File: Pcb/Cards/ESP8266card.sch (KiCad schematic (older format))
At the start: 16 parts, among them P1 Debug-SoftSerial-FTDI, P2 ESP-Programming-FTDI, P3 CA6_CONN_01X10, U1 ESP-12E/F

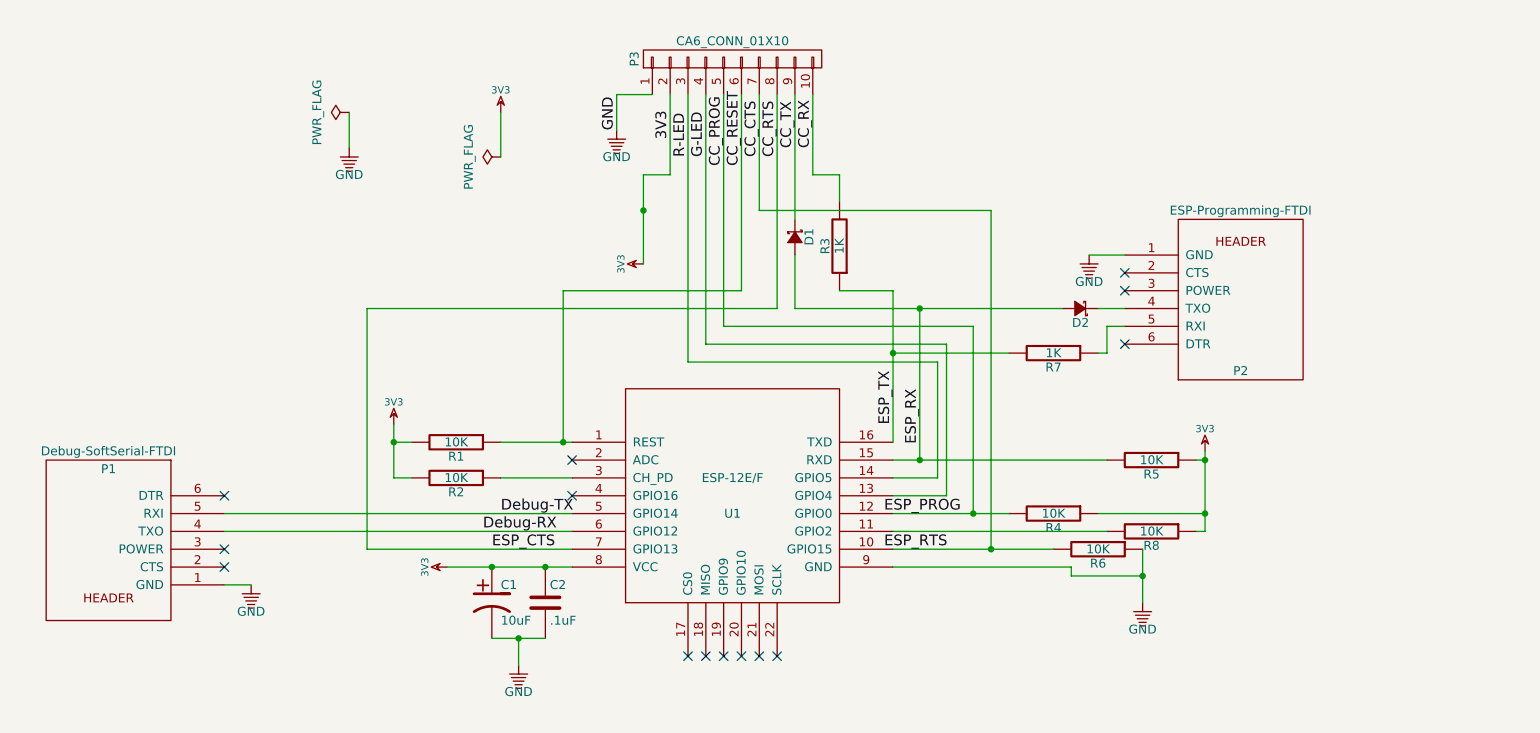
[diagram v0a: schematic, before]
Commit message: 1st commit with completed schematic and routed board.  Added 1K on ESP RX back in (easy to short later if it causes problems). Used 12 mil Power & Gnd and 6 mil remaining traces.  1x10 CA6_Com_connector is properly on the bottom, but FTDI headers and unpopulated.  We'll need to check that case has room when they are populated.  I wasn't sure how to get air-wires for Gnd's on headers to go away, so I added via's on the pin and separately (check and correct if needed).  Card outline is .05" less than CA6 board on the right and bottom for case clearance.  Did not start gerber process.
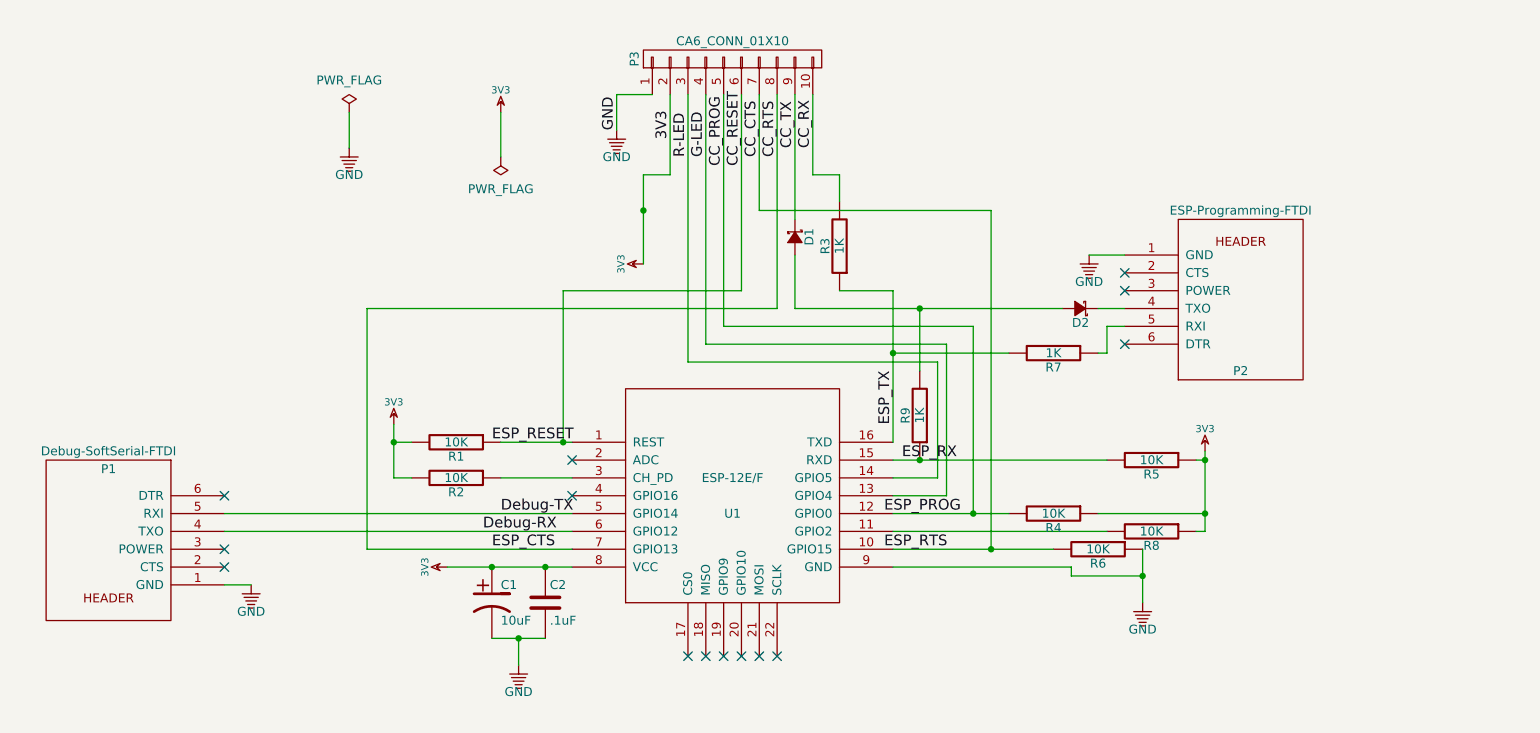
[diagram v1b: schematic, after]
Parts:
- added R9: 1K, CA6:SM0603_Resistor, symbol R
- U1: footprint CA6:ESP-12E -> CA6:ESP-12E-F-no-bottom-pads
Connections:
- net ESP_RX: now also R9.1; no longer D1.2 (A), D2.2 (A)
- new net: D1.2 (A), D2.2 (A), R9.2
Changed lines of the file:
@@
 LIBS:contrib
 LIBS:valves
-LIBS:w_rtx
-LIBS:ESP8266
-LIBS:74xgxx
-LIBS:ac-dc
-LIBS:actel
-LIBS:allegro
-LIBS:Altera
-LIBS:analog_devices
-LIBS:battery_management
-LIBS:bbd
-LIBS:bosch
-LIBS:brooktre
-LIBS:cmos_ieee
-LIBS:dc-dc
-LIBS:diode
-LIBS:elec-unifil
-LIBS:ESD_Protection
-LIBS:ftdi
-LIBS:gennum
-LIBS:graphic
-LIBS:hc11
-LIBS:ir
-LIBS:Lattice
-LIBS:logo
-LIBS:maxim
-LIBS:mechanical
-LIBS:microchip_dspic33dsc
-LIBS:microchip_pic10mcu
-LIBS:microchip_pic12mcu
-LIBS:microchip_pic16mcu
-LIBS:microchip_pic18mcu
-LIBS:microchip_pic32mcu
-LIBS:motor_drivers
-LIBS:motors
-LIBS:msp430
-LIBS:nordicsemi
-LIBS:NXP
-LIBS:nxp_1
-LIBS:nxp_armmcu
-LIBS:onsemi
-LIBS:Oscillators
-LIBS:Power_Management
-LIBS:powerint
-LIBS:pspice
-LIBS:references
-LIBS:relays
-LIBS:rfcom
-LIBS:sensors
-LIBS:silabs
-LIBS:stm8
-LIBS:stm32
-LIBS:supertex
-LIBS:switches
-LIBS:transf
-LIBS:triac_thyristor
-LIBS:ttl_ieee
-LIBS:video
-LIBS:wiznet
-LIBS:Worldsemi
-LIBS:Xicor
-LIBS:zetex
-LIBS:Zilog
 LIBS:ESP8266card-cache
 EELAYER 25 0
@@
 	7650 2900 7500 2900
 Wire Wire Line
-	3550 3550 3550 3650
-Wire Wire Line
-	3550 3650 3550 3850
+	3550 3550 3550 3850
 Connection ~ 3550 3650
 $Comp
@@
 $EndComp
 Wire Wire Line
-	7750 4250 7750 4400
-Wire Wire Line
-	7750 4400 7750 4550
+	7750 4250 7750 4550
 $Comp
 L R R8
@@
 $EndComp
 Wire Wire Line
-	8100 3700 8100 3750
-Wire Wire Line
-	8100 3750 8100 4050
-Wire Wire Line
-	8100 4050 8100 4150
+	8100 3700 8100 4150
 Connection ~ 8100 4050
 Connection ~ 8100 3750
@@
 $EndComp
 Wire Wire Line
-	3850 4350 4100 4350
-Wire Wire Line
-	4100 4350 4400 4350
-Wire Wire Line
-	4400 4350 4550 4350
+	3850 4350 4550 4350
 Connection ~ 4400 4350
 Wire Wire Line
-	4100 4750 4250 4750
-Wire Wire Line
-	4250 4750 4400 4750
+	4100 4750 4400 4750
 $Comp
 L GND #PWR04
@@
 F 3 "" H 4150 2050 50  0000 C CNN
 	1    4150 2050
-	0    -1   -1   0
+	-1   0    0    1
 $EndComp
 $Comp
@@
 	5200 1700 5200 3200
 Wire Wire Line
-	6350 2800 6350 3150
-Wire Wire Line
-	6350 3150 6350 3650
+	6350 2800 6350 3650
 Text Label 6350 3550 1    60   ~ 0
 ESP_TX
@@
 NoConn ~ 2600 4350
 Connection ~ 6500 3750
-Text Label 6500 3350 3    60   ~ 0
-ESP_RX
 Wire Wire Line
 	5000 1700 4800 1700
@@
 	5100 2150 4950 2150
 Wire Wire Line
-	4950 2150 4950 2350
-Wire Wire Line
-	4950 2350 4950 2650
+	4950 2150 4950 2650
 Connection ~ 4950 2350
 Wire Wire Line
@@
 	6350 2800 6050 2800
 Wire Wire Line
-	5800 2900 6500 2900
-Wire Wire Line
-	6500 2900 7300 2900
+	5800 2900 7300 2900
 Connection ~ 6500 2900
 Wire Wire Line
 	5800 2600 5800 2900
-Wire Wire Line
-	6500 3750 6500 2900
 Wire Wire Line
 	6350 3850 6600 3850
@@
 F 0 "U1" H 5450 3850 50  0000 C CNN
 F 1 "ESP-12E/F" H 5450 4050 50  0000 C CNN
-F 2 "CA6:ESP-12E" H 5450 3950 50  0001 C CNN
+F 2 "CA6:ESP-12E-F-no-bottom-pads" H 5450 3950 50  0001 C CNN
 F 3 "" H 5450 3950 50  0001 C CNN
 	1    5450 3950
@@
 	6050 2150 6050 2300
 Wire Wire Line
-	6350 4250 6900 4250
-Wire Wire Line
-	6900 4250 7250 4250
+	6350 4250 7250 4250
 Wire Wire Line
 	3650 3650 3550 3650
@@
 	4550 3850 4150 3850
 Wire Wire Line
-	4150 3650 4500 3650
-Wire Wire Line
-	4500 3650 4550 3650
+	4150 3650 4550 3650
 Wire Wire Line
 	8050 3750 8100 3750
 Wire Wire Line
-	6350 3750 6500 3750
-Wire Wire Line
-	6500 3750 7550 3750
+	6350 3750 7550 3750
 Wire Wire Line
 	7500 4050 8100 4050
 Wire Wire Line
-	6350 4050 6800 4050
-Wire Wire Line
-	6800 4050 7000 4050
+	6350 4050 7000 4050
 Wire Wire Line
 	5900 1700 5900 2150
@@
 F 3 "" H 3300 1800 50  0000 C CNN
 	1    3300 1800
-	0    -1   -1   0
+	1    0    0    -1
 $EndComp
 $Comp
@@
 	1    0    0    -1
 $EndComp
+$Comp
+L R R9
+U 1 1 58C41CF1
+P 6500 3500
+F 0 "R9" V 6580 3500 50  0000 C CNN
+F 1 "1K" V 6500 3500 50  0000 C CNN
+F 2 "CA6:SM0603_Resistor" V 6430 3500 50  0001 C CNN
+F 3 "" H 6500 3500 50  0000 C CNN
+	1    6500 3500
+	-1   0    0    1
+$EndComp
+Wire Wire Line
+	6500 3250 6500 2900
+Text Label 6400 3750 0    60   ~ 0
+ESP_RX
+Text Label 4100 3650 0    60   ~ 0
+ESP_RESET
 $EndSCHEMATC

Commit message: Fix some drc issues
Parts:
- P2: symbol FTDI -> FTDI-RESCUE-ESP8266card
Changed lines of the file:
@@
 EESchema Schematic File Version 2
+LIBS:ESP8266card-rescue
 LIBS:CA6
 LIBS:power
@@
 $EndComp
 $Comp
-L FTDI P2
+L FTDI-RESCUE-ESP8266card P2
 U 1 1 58C10A25
 P 8300 2850
@@
 L GND #PWR02
 U 1 1 58C14094
-P 4800 1900
-F 0 "#PWR02" H 4800 1650 50  0001 C CNN
-F 1 "GND" H 4800 1750 50  0000 C CNN
-F 2 "" H 4800 1900 50  0000 C CNN
-F 3 "" H 4800 1900 50  0000 C CNN
-	1    4800 1900
+P 4950 1900
+F 0 "#PWR02" H 4950 1650 50  0001 C CNN
+F 1 "GND" H 4950 1750 50  0000 C CNN
+F 2 "" H 4950 1900 50  0000 C CNN
+F 3 "" H 4950 1900 50  0000 C CNN
+	1    4950 1900
 	1    0    0    -1
 $EndComp
@@
 Connection ~ 4100 4350
 $Comp
-L PWR_FLAG #FLG05
-U 1 1 58C165F7
-P 4150 2050
-F 0 "#FLG05" H 4150 2145 50  0001 C CNN
-F 1 "PWR_FLAG" H 4150 2230 50  0000 C CNN
-F 2 "" H 4150 2050 50  0000 C CNN
-F 3 "" H 4150 2050 50  0000 C CNN
-	1    4150 2050
-	-1   0    0    1
-$EndComp
-$Comp
 L CONN_01X10 P3
 U 1 1 58BE5BC6
@@
 $EndComp
 Wire Wire Line
-	5100 1700 5100 2150
+	5100 2150 5100 1700
 Wire Wire Line
 	5300 1700 5300 3100
@@
 Wire Wire Line
 	5800 1700 5800 2400
-Text Label 4800 1900 1    60   ~ 0
-GND
-Text Label 5100 1950 1    60   ~ 0
-3V3
-Text Label 5900 2000 1    60   ~ 0
+Text Label 5900 2100 1    60   ~ 0
 CC_RX
-Text Label 5200 2050 1    60   ~ 0
+Text Label 5200 2100 1    60   ~ 0
 R-LED
-Text Label 5800 2000 1    60   ~ 0
+Text Label 5800 2100 1    60   ~ 0
 CC_TX
-Text Label 5300 2050 1    60   ~ 0
+Text Label 5300 2100 1    60   ~ 0
 G-LED
-Text Label 5700 2050 1    60   ~ 0
+Text Label 5700 2100 1    60   ~ 0
 CC_RTS
 Text Label 5500 2100 1    60   ~ 0
 CC_RESET
-Text Label 5600 2050 1    60   ~ 0
+Text Label 5600 2100 1    60   ~ 0
 CC_CTS
 Text Label 5400 2100 1    60   ~ 0
@@
 P 1950 4200
 F 0 "P1" H 1950 3800 50  0000 C CNN
-F 1 "Debug-SoftSerial-FTDI" H 1950 3700 50  0000 C CNN
+F 1 "Debug-SoftSerial-FTDI" H 1950 4600 50  0000 C CNN
 F 2 "CA6:SIL-6" H 1950 4200 50  0001 C CNN
 F 3 "DOCUMENTATION" H 1950 4200 50  0001 C CNN
@@
 	2600 4050 4550 4050
 $Comp
-L GND #PWR06
+L GND #PWR05
 U 1 1 58BF45F7
 P 2750 4450
-F 0 "#PWR06" H 2750 4200 50  0001 C CNN
+F 0 "#PWR05" H 2750 4200 50  0001 C CNN
 F 1 "GND" H 2750 4300 50  0000 C CNN
 F 2 "" H 2750 4450 50  0000 C CNN
@@
 	1    0    0    -1
 $EndComp
-Wire Wire Line
-	2750 4450 2600 4450
 Text Label 4150 4050 0    60   ~ 0
 Debug-TX
@@
 Connection ~ 6500 3750
 Wire Wire Line
-	5000 1700 4800 1700
-Wire Wire Line
-	4800 1700 4800 1900
-Wire Wire Line
-	5100 2150 4950 2150
-Wire Wire Line
-	4950 2150 4950 2650
-Connection ~ 4950 2350
+	5000 1700 4950 1700
+Wire Wire Line
+	4950 1700 4950 1900
+Wire Wire Line
+	4950 2150 5100 2150
 Wire Wire Line
 	5900 2150 6050 2150
@@
 	-1   0    0    1
 $EndComp
-$Comp
-L GND #PWR07
-U 1 1 58C2E8B7
-P 3300 2000
-F 0 "#PWR07" H 3300 1750 50  0001 C CNN
-F 1 "GND" H 3300 1850 50  0000 C CNN
-F 2 "" H 3300 2000 50  0000 C CNN
-F 3 "" H 3300 2000 50  0000 C CNN
-	1    3300 2000
-	1    0    0    -1
-$EndComp
-Wire Wire Line
-	4150 1800 4150 2050
-Wire Wire Line
-	3300 1800 3300 2000
 Wire Wire Line
 	7550 4150 6350 4150
@@
 	8100 4150 8050 4150
 $Comp
-L PWR_FLAG #FLG08
-U 1 1 58C32C54
-P 3300 1800
-F 0 "#FLG08" H 3300 1895 50  0001 C CNN
-F 1 "PWR_FLAG" H 3300 1980 50  0000 C CNN
-F 2 "" H 3300 1800 50  0000 C CNN
-F 3 "" H 3300 1800 50  0000 C CNN
-	1    3300 1800
-	1    0    0    -1
-$EndComp
-$Comp
-L 3V3 #PWR09
+L 3V3 #PWR06
 U 1 1 58C32ED5
-P 4950 2650
-F 0 "#PWR09" H 4950 2750 40  0001 C CNN
-F 1 "3V3" H 4950 2775 40  0000 C CNN
-F 2 "" H 4950 2650 60  0000 C CNN
-F 3 "" H 4950 2650 60  0000 C CNN
-	1    4950 2650
+P 4950 2150
+F 0 "#PWR06" H 4950 2250 40  0001 C CNN
+F 1 "3V3" H 4950 2275 40  0000 C CNN
+F 2 "" H 4950 2150 60  0000 C CNN
+F 3 "" H 4950 2150 60  0000 C CNN
+	1    4950 2150
 	0    -1   -1   0
 $EndComp
 $Comp
-L 3V3 #PWR010
-U 1 1 58C33748
-P 4150 1800
-F 0 "#PWR010" H 4150 1900 40  0001 C CNN
-F 1 "3V3" H 4150 1925 40  0000 C CNN
-F 2 "" H 4150 1800 60  0000 C CNN
-F 3 "" H 4150 1800 60  0000 C CNN
-	1    4150 1800
-	1    0    0    -1
-$EndComp
-$Comp
-L 3V3 #PWR011
+L 3V3 #PWR07
 U 1 1 58C341AF
 P 3550 3550
-F 0 "#PWR011" H 3550 3650 40  0001 C CNN
+F 0 "#PWR07" H 3550 3650 40  0001 C CNN
 F 1 "3V3" H 3550 3675 40  0000 C CNN
 F 2 "" H 3550 3550 60  0000 C CNN
@@
 $EndComp
 $Comp
-L 3V3 #PWR012
+L 3V3 #PWR08
 U 1 1 58C34BCB
 P 3850 4350
-F 0 "#PWR012" H 3850 4450 40  0001 C CNN
+F 0 "#PWR08" H 3850 4450 40  0001 C CNN
 F 1 "3V3" H 3850 4475 40  0000 C CNN
 F 2 "" H 3850 4350 60  0000 C CNN
@@
 $EndComp
 $Comp
-L 3V3 #PWR013
+L 3V3 #PWR09
 U 1 1 58C34C97
 P 8100 3700
-F 0 "#PWR013" H 8100 3800 40  0001 C CNN
+F 0 "#PWR09" H 8100 3800 40  0001 C CNN
 F 1 "3V3" H 8100 3825 40  0000 C CNN
 F 2 "" H 8100 3700 60  0000 C CNN
@@
 Text Label 4100 3650 0    60   ~ 0
 ESP_RESET
+Wire Wire Line
+	2750 4450 2600 4450
 $EndSCHEMATC

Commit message: Eliminated ground pour, changed FTDI headers to angled, corrected ESP-12E/F-no-bottom-pads to SMD pads, improved spacing near antenna, moved and shrank some text values
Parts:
- P1, P2: footprint CA6:SIL-6 -> Pin_Headers:Pin_Header_Angled_1x06_Pitch2.54mm
- P3: footprint Pin_Headers:Pin_Header_Straight_1x10_Pitch2.54mm -> Pin_Header_Straight_1x10_Pitch2.54mm
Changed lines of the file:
@@
 F 0 "P2" H 8300 2450 50  0000 C CNN
 F 1 "ESP-Programming-FTDI" H 8300 3350 50  0000 C CNN
-F 2 "CA6:SIL-6" H 8300 2850 50  0001 C CNN
+F 2 "Pin_Headers:Pin_Header_Angled_1x06_Pitch2.54mm" H 8300 2850 50  0001 C CNN
 F 3 "DOCUMENTATION" H 8300 2850 50  0001 C CNN
 	1    8300 2850
@@
 F 0 "P3" H 5450 2050 50  0000 C CNN
 F 1 "CA6_CONN_01X10" V 5550 1500 50  0000 C CNN
-F 2 "Pin_Headers:Pin_Header_Straight_1x10_Pitch2.54mm" H 5450 1500 50  0001 C CNN
+F 2 "Pin_Header_Straight_1x10_Pitch2.54mm" H 5450 1500 50  0001 C CNN
 F 3 "" H 5450 1500 50  0000 C CNN
 	1    5450 1500
@@
 F 0 "P1" H 1950 3800 50  0000 C CNN
 F 1 "Debug-SoftSerial-FTDI" H 1950 4600 50  0000 C CNN
-F 2 "CA6:SIL-6" H 1950 4200 50  0001 C CNN
+F 2 "Pin_Headers:Pin_Header_Angled_1x06_Pitch2.54mm" H 1950 4200 50  0001 C CNN
 F 3 "DOCUMENTATION" H 1950 4200 50  0001 C CNN
 	1    1950 4200

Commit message: Got rid of old 1x10 version and renamed cards2 to card, also fixed one text field
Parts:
- removed D1, D2: diode_schottky_20V_1A, CA6:DO-214AC(SMA), symbol diode_schottky_20V_1A
- removed P1: Debug-SoftSerial-FTDI, Pin_Headers:Pin_Header_Angled_1x06_Pitch2.54mm, symbol FTDI
- removed P3: CA6_CONN_01X10, Pin_Header_Straight_1x10_Pitch2.54mm, symbol CONN_01X10
- removed R3, R7, R9: 1K, CA6:SM0603_Resistor, symbol R
- removed R5: 10K, CA6:SM0603_Resistor, symbol R
- added J1: Debug_TX, CA6:Pin_Header_Angled_1x02_Pitch2.54mm, symbol CONN_01X02
- added J2: CA6_02X06, CA6:Pin_Header_Straight_2x06_Pitch2.54mm, symbol CONN_02X06
- added U1: SN74AHC1G08, CA6:SOT-23-5_GATE, symbol SN74AHC1G08
- added X1: HOLE, CA6:HOLE_3.0mm, symbol HOLE
- P1: renamed from P2; symbol FTDI-RESCUE-ESP8266card -> FTDI
- R3: renamed from R4; value 10K -> 4.7k
- R5: renamed from R1; value 10K -> 4.7k
- renumbered C2 to C1, C1 to C2, R8 to R1, R6 to R2, R2 to R4, U1 to U2
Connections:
- net ESP_TX is gone; now on net CC_RX: U2.16 (TXD)
- net 3V3: now also J2.2 (P2), U1.5 (VCC)
- net CC_CTS: now also J2.7 (P7)
- net CC_PROG: now also J2.5 (P5)
- net CC_RESET: now also J2.6 (P6)
- net CC_RTS: now also J2.8 (P8)
- net CC_RX: now also P1.5 (RXI), J2.10 (P10)
- net CC_TX: now also J2.9 (P9), U1.1
- net Debug-TX: now also R1.2, U2.11 (GPIO2), J1.2 (P2); no longer U2.5 (GPIO14)
- net ESP_RX: now also U1.4
- net GND: now also J1.1 (P1), J2.1 (P1), U1.3 (GND)
- net FTDI_TX: now reaches P1.4 (TXO)
- net FTDI_TX: now also U1.2
- net Debug-RX renamed CC_EXT1
- net CC_EXT1: now also J2.11 (P11)
- net G-LED renamed CC_G_LED
- net CC_G_LED: now also J2.4 (P4)
- net R-LED renamed CC_R_LED
- net CC_R_LED: now also J2.3 (P3)
- new net CC_EXT0: J2.12 (P12), U2.5 (GPIO14)
- no-connect marks 14 -> 11
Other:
- moved on the sheet: C1, C2, P1, R1, R2, R3, R4, R5, U2

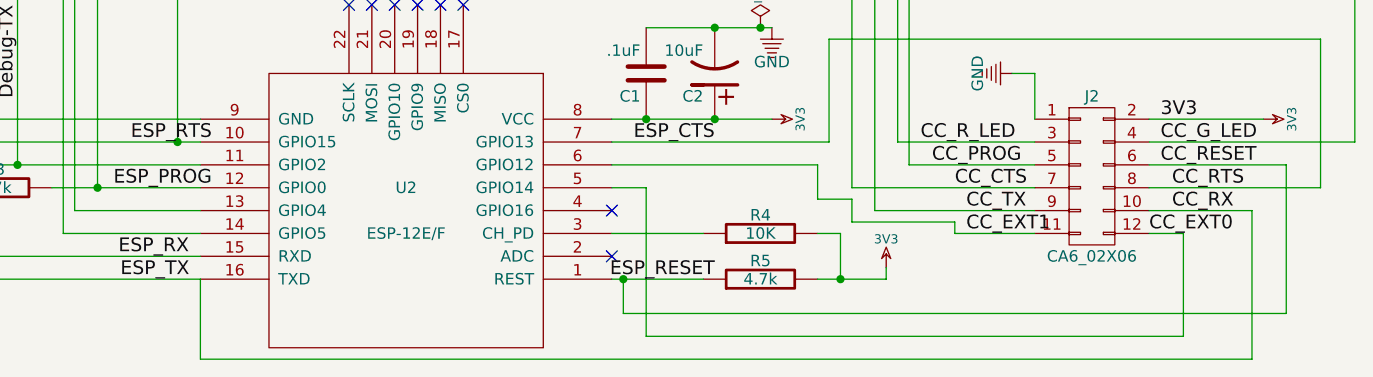
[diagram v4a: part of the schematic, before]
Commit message: corrected labelling of EXT pins on both nRF52card and ESP8266card and rerouted some traces on nRF52card for better ground pour.
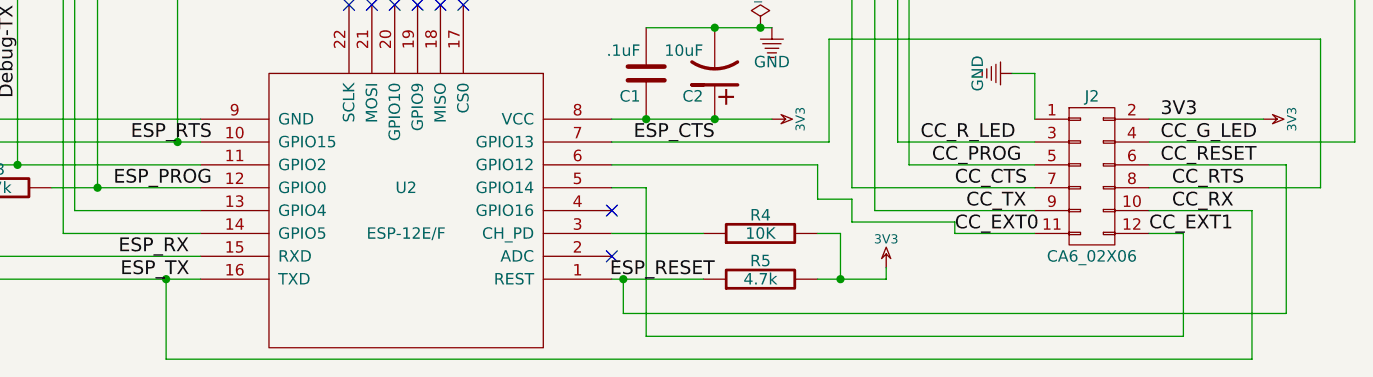
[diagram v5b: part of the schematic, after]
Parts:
- P1: footprint Pin_Headers:Pin_Header_Angled_1x06_Pitch2.54mm -> CA6:Pin_Header_Angled_1x06_Pitch2.54mm
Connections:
- net CC_EXT0: now also J2.11 (P11), U2.6 (GPIO12); no longer J2.12 (P12), U2.5 (GPIO14)
- net CC_EXT1: now also J2.12 (P12), U2.5 (GPIO14); no longer J2.11 (P11), U2.6 (GPIO12)
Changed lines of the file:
@@
 EESchema Schematic File Version 2
-LIBS:ESP8266card-rescue
 LIBS:CA6
 LIBS:power
@@
 LIBS:contrib
 LIBS:valves
-LIBS:ESP8266card2-cache
+LIBS:ESP8266card-cache
 EELAYER 25 0
 EELAYER END
@@
 F 0 "P1" H 5700 1300 50  0000 C CNN
 F 1 "ESP-Programming-FTDI" V 6100 1700 50  0000 C CNN
-F 2 "Pin_Headers:Pin_Header_Angled_1x06_Pitch2.54mm" H 5700 1700 50  0001 C CNN
+F 2 "CA6:Pin_Header_Angled_1x06_Pitch2.54mm" H 5700 1700 50  0001 C CNN
 F 3 "DOCUMENTATION" H 5700 1700 50  0001 C CNN
 	1    5700 1700
@@
 	5750 2750 5250 2750
 Wire Wire Line
-	4850 4850 4850 5200
-Wire Wire Line
-	4850 5200 9450 5200
+	4700 5200 9450 5200
 Wire Wire Line
 	9450 5200 9450 4550
@@
 Wire Wire Line
 	8150 4650 8500 4650
-Text Label 8200 4650 0    60   ~ 0
+Text Label 8150 4650 0    60   ~ 0
+CC_EXT0
+Text Label 9000 4650 0    60   ~ 0
 CC_EXT1
-Text Label 9000 4650 0    60   ~ 0
-CC_EXT0
 Wire Wire Line
 	5850 2450 5850 2350
@@
 Text Label 3700 2850 0    60   ~ 0
 ESP_RX
+Wire Wire Line
+	4700 5200 4700 4850
+Connection ~ 4700 4850
 $EndSCHEMATC
